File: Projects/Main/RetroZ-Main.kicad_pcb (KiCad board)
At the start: 2 copper layers, 100 x 80 mm, 22 parts, among them J1 PJ-102A, J2 Master Bus, SW1 On/Off, SW2 RESET, U1 74HCT04, U2 L7805CV-DG, U3 Z80CPU, U4 max699cpa, Y1 7.3728Mhz

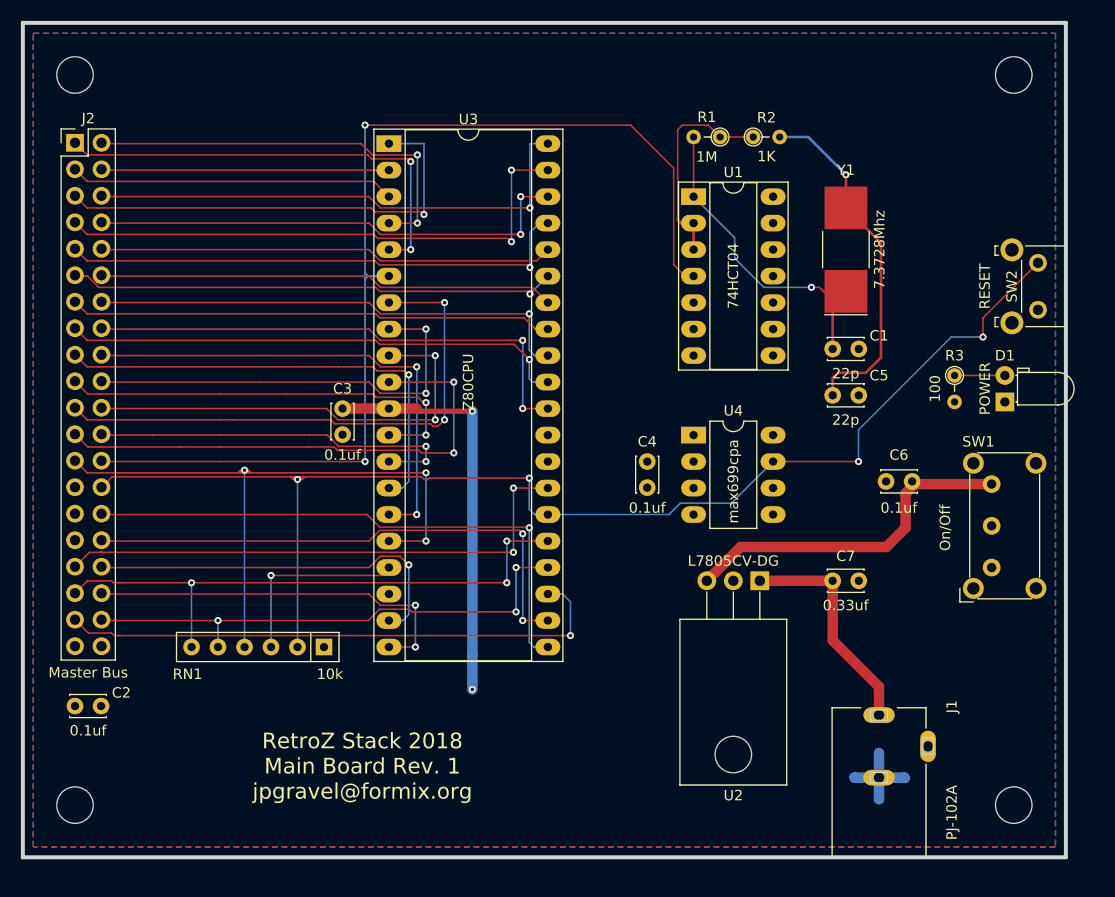
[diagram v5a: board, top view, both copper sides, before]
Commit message: fixed a bunch of issues with the main board and some on the memory board
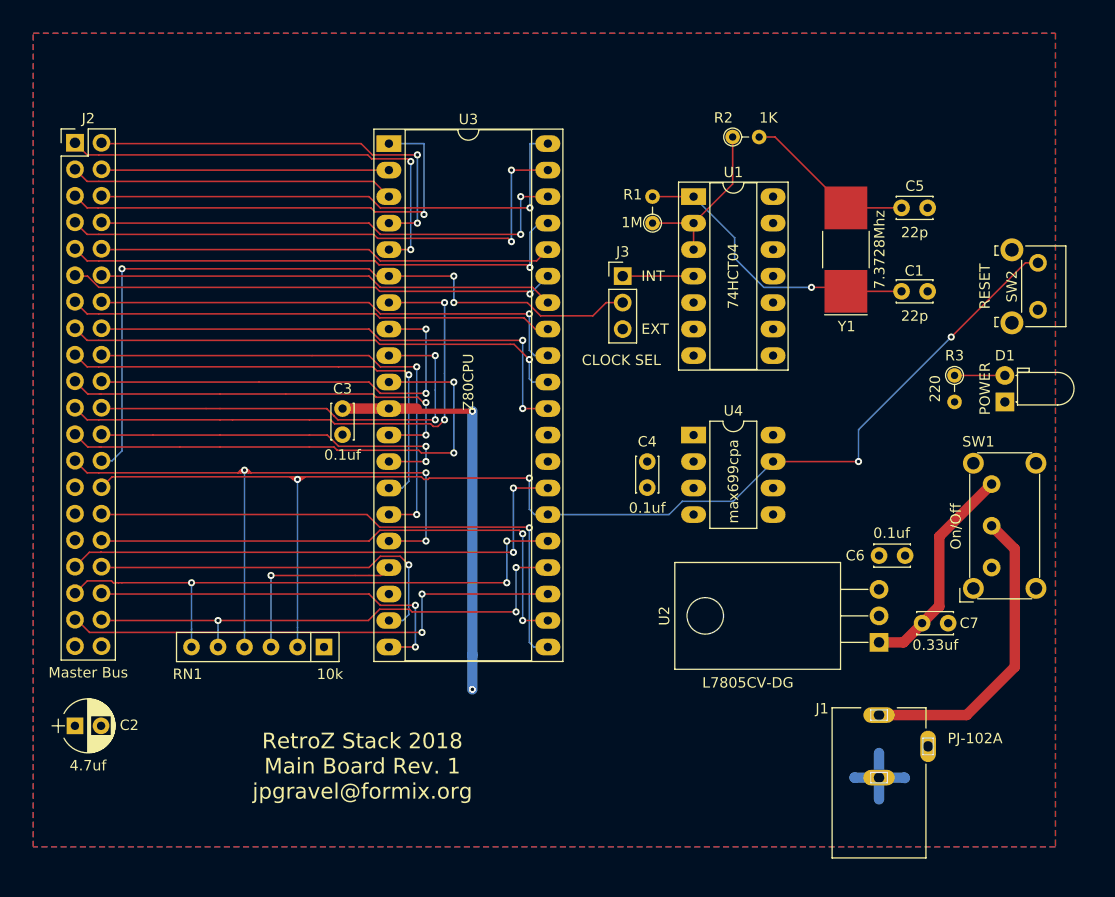
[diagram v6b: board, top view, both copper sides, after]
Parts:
- removed REF**: EuroBoard_halb_Type-I_100mmX80mm_holes, EuroBoard_Outline:EuroBoard_halb_Type-I_100mmX80mm_holes
- added J3: CLOCK SEL, Pin_Headers:Pin_Header_Straight_1x03_Pitch2.54mm, F.Cu at (147.5, 81.3)
- C2: value 0.1uf -> 4.7uf; footprint Capacitors_THT:C_Disc_D3.4mm_W2.1mm_P2.50mm -> Capacitors_THT:CP_Radial_D5.0mm_P2.50mm
- R3: value 100 -> 220
- moved C5 19.1 mm to (174.2, 74.7)
- moved U2 12.9 mm to (172.1, 116.4), turned to 90 degrees
- moved R1 10.5 mm to (150.4, 76.2), turned to 90 degrees
- moved C7 9.49 mm to (176.2, 114.6)
- moved C1 8.61 mm to (174.2, 82.7)
- moved C6 7.79 mm to (172.1, 108.1), turned to 0 degrees
- moved R2 1.97 mm to (158.1, 67.9)
- moved C2 1.90 mm to (95.0, 124.4)
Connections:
- C6 pad 1: Net-(C6-Pad1) -> VCC
- J1 pad 1: Net-(C7-Pad1) -> Net-(J1-Pad1)
- SW1 pad 2: VCC -> Net-(J1-Pad1)
- SW1 pad 3: Net-(C6-Pad1) -> Net-(C7-Pad1)
- U1 pad 4: CLK -> Net-(J3-Pad1)
- U2 pad 3: Net-(C6-Pad1) -> VCC
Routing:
- net Net-(C6-Pad1): track 33.1 -> 0.00 mm
- net CLK: track 103.8 -> 71.7 mm, vias 2 -> 3
- net Net-(J1-Pad1): track 0.00 -> 29.4 mm
- net Net-(C5-Pad1): track 34.3 -> 16.5 mm, vias 1 -> 0
- net Net-(J3-Pad1): track 0.00 -> 7.68 mm
- net ~BUSACK: track 53.9 -> 49.5 mm, vias 1 -> 2
- net Net-(R1-Pad1): track 20.7 -> 17.2 mm
- net ~RESET: track 125.5 -> 124.4 mm
- net Net-(C1-Pad1): track 31.8 -> 31.1 mm
- net Net-(C7-Pad1): track 21.7 -> 21.1 mm
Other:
- board size 100 x 80 mm -> 6 x 7 mm
- board text added: "EXT"
- board text added: "INT"

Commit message: changed power-on reser chip
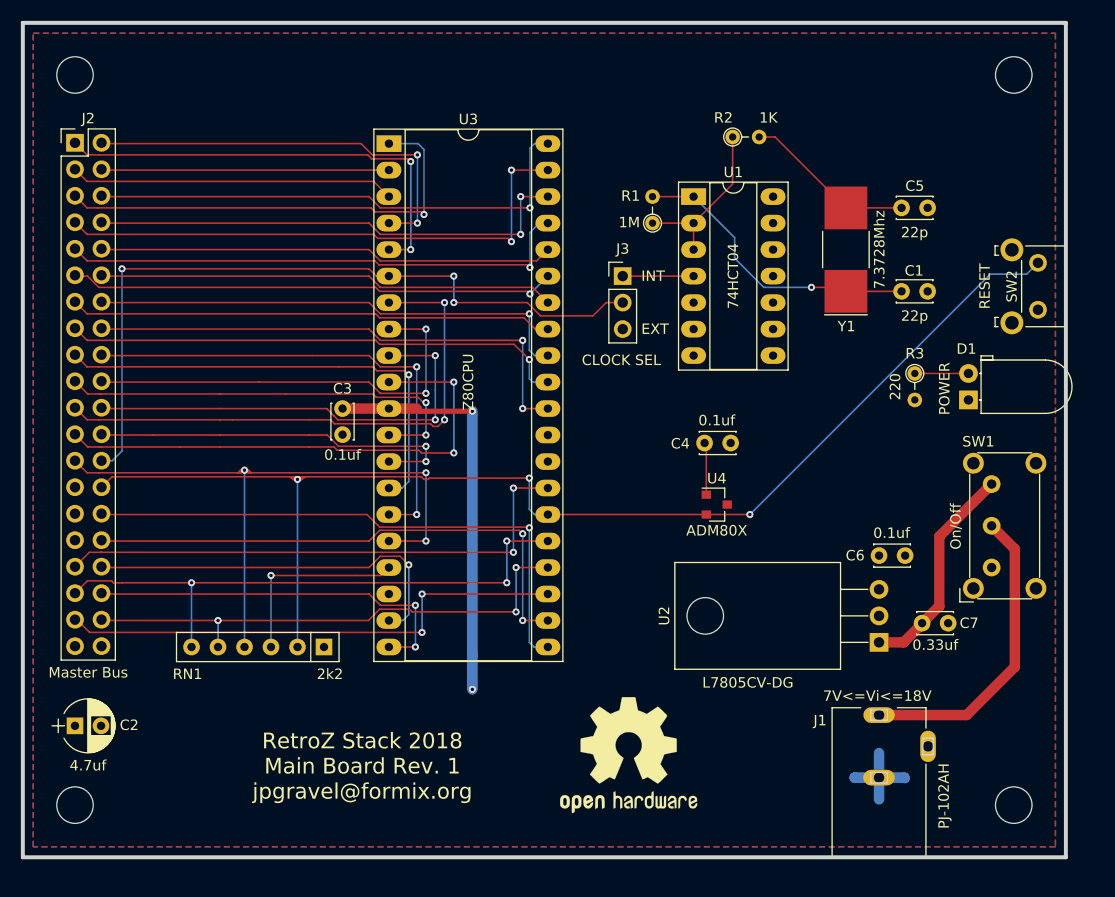
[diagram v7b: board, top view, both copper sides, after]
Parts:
- added REF**: EuroBoard_halb_Type-I_100mmX80mm_holes, EuroBoard_Outline:EuroBoard_halb_Type-I_100mmX80mm_holes, F.Cu at (90.0, 137.0)
- added REF***: OSHW-Logo2_14.6x12mm_SilkScreen, Symbols:OSHW-Logo2_14.6x12mm_SilkScreen, F.Cu at (148.1, 127.2)
- D1: footprint LEDs:LED_D3.0mm_Horizontal_O1.27mm_Z2.0mm -> LEDs:LED_D5.0mm_Horizontal_O1.27mm_Z3.0mm
- J1: value PJ-102A -> PJ-102AH
- RN1: value 10k -> 2k2
- U4: value max699cpa -> ADM80X; footprint Housings_DIP:DIP-8_W7.62mm_LongPads -> TO_SOT_Packages_SMD:SOT-23
- moved C4 8.20 mm to (157.9, 97.3), turned to 180 degrees
- moved U4 7.03 mm to (156.5, 103.2)
- moved R3 3.81 mm to (175.5, 90.6)
- moved D1 3.50 mm to (180.7, 93.2)
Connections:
- U4 pad 1: VCC -> GND
- U4 pad 2: VCC -> ~RESET
- U4 pad 3: GND -> VCC
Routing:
- net GND: track 9.30 -> 14.3 mm
- net ~RESET: track 124.4 -> 122.6 mm, vias 4 -> 3
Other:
- board size 6 x 7 mm -> 100 x 80 mm
- board text added: "7V<=Vi<=18V"

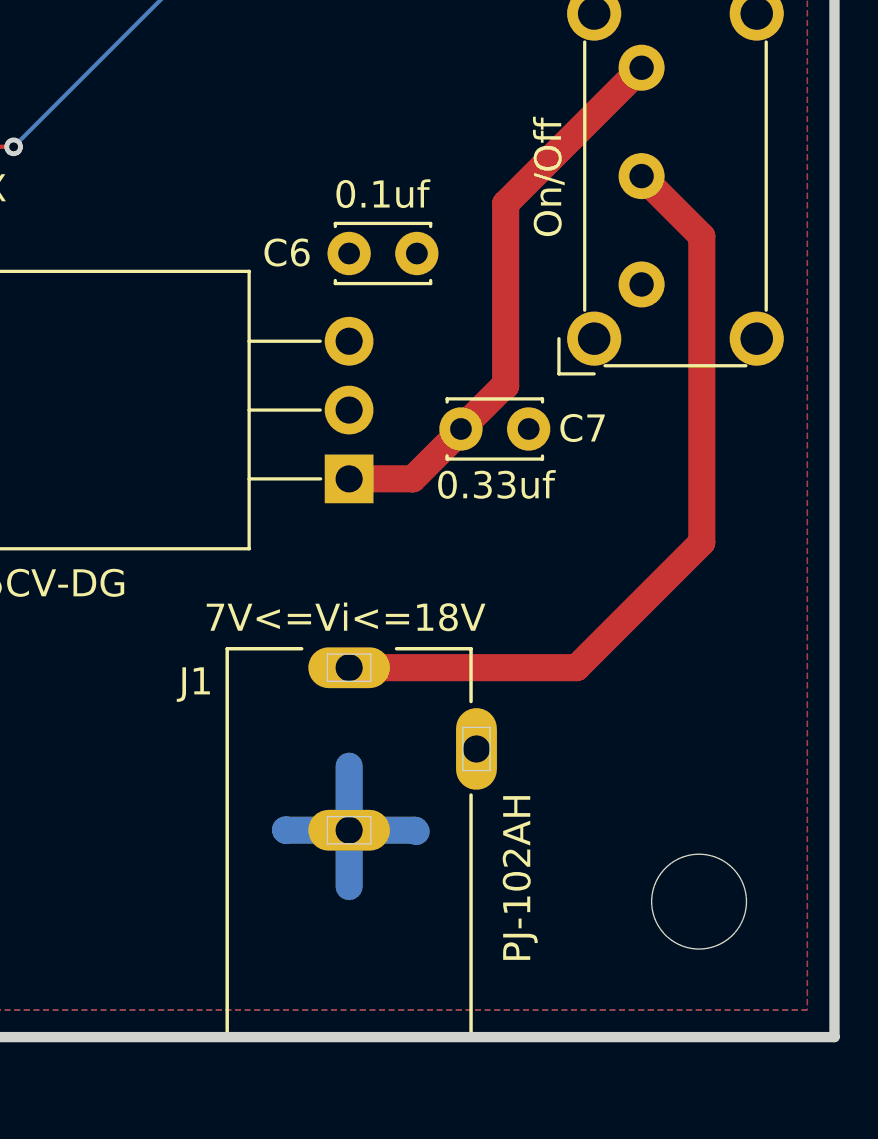
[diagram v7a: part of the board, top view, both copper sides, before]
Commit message: fixing memory access time
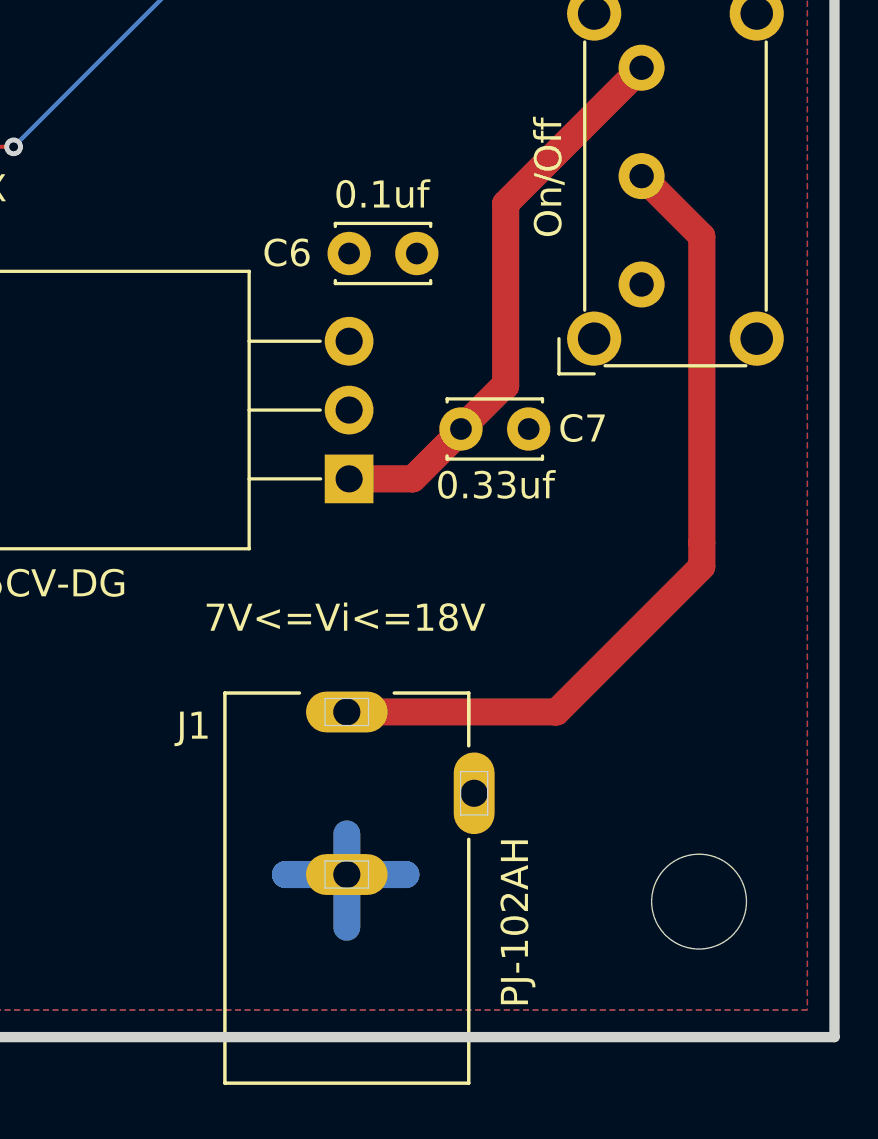
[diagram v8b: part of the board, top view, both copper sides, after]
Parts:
- moved J1 1.64 mm to (172.0, 128.0)
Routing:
- net GND: track 14.3 -> 12.9 mm
- net Net-(J1-Pad1): track 29.4 -> 30.7 mm
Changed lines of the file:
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@@
     (thickness 1.6)
     (drawings 4)
-    (tracks 432)
+    (tracks 433)
     (zones 0)
     (modules 24)
@@
   )
   (setup
-    (last_trace_width 0.1524)
+    (last_trace_width 1)
     (user_trace_width 0.254)
     (user_trace_width 0.5)
@@
       (drillshape 0)
       (scaleselection 1)
-      (outputdirectory ../plots/RetroZ-Main))
+      (outputdirectory ../../plots/RetroZ-Main/))
   )
   (net 0 "")
@@
   )
   (module PJ-102A:CUI_PJ-102A (layer Top)
-    (at 172.085 126.365 180)
+    (at 172 128 180)
     (fp_text reference J1 (at 5.6515 2.4765 360) (layer F.SilkS)
       (effects (font (size 1 1) (thickness 0.15)))
@@
   (segment (start 167.64 84.01) (end 168.91 82.74) (width 0.254) (layer Top) (net 1))
   (segment (start 168.5295 82.3595) (end 168.91 82.74) (width 0.254) (layer Top) (net 1))
+  (segment (start 172 131) (end 169.736 131) (width 1) (layer Bottom) (net 2) (status 400000))
+  (segment (start 169.736 131) (end 169.7355 131.0005) (width 1) (layer Bottom) (net 2))
+  (segment (start 172 131) (end 174.18 131) (width 1) (layer Bottom) (net 2) (status 400000))
+  (segment (start 174.18 131) (end 174.1805 131.0005) (width 1) (layer Bottom) (net 2))
+  (segment (start 172 131) (end 172 132.9475) (width 1) (layer Bottom) (net 2) (status 400000))
+  (segment (start 172 131) (end 172 129.498) (width 1) (layer Bottom) (net 2) (status 400000))
   (segment (start 155.5275 102.2375) (end 155.5275 97.4485) (width 0.1524) (layer Top) (net 2))
   (segment (start 155.5275 97.4485) (end 155.361 97.282) (width 0.1524) (layer Top) (net 2))
-  (segment (start 172.085 129.365) (end 169.751 129.365) (width 1) (layer Bottom) (net 2))
-  (segment (start 169.751 129.365) (end 169.7355 129.3495) (width 1) (layer Bottom) (net 2))
-  (segment (start 172.085 129.365) (end 174.5135 129.365) (width 1) (layer Bottom) (net 2))
-  (segment (start 174.5135 129.365) (end 174.5615 129.413) (width 1) (layer Bottom) (net 2))
-  (segment (start 172.085 129.365) (end 172.085 131.445) (width 1) (layer Bottom) (net 2))
-  (segment (start 172.085 129.365) (end 172.085 127) (width 1) (layer Bottom) (net 2))
   (segment (start 125.095 93.98) (end 127.762 93.98) (width 1) (layer Top) (net 3))
   (via (at 133.096 120.904) (size 0.6858) (drill 0.3302) (layers Top Bottom) (net 3))
@@
   (segment (start 113.792 116.84) (end 113.792 109.982) (width 0.1524) (layer Bottom) (net 50))
   (segment (start 124.333 109.982) (end 125.095 109.22) (width 0.1524) (layer Top) (net 50))
-  (segment (start 172.085 123.365) (end 180.4825 123.365) (width 1) (layer Top) (net 51))
-  (segment (start 185.1025 107.4425) (end 182.88 105.22) (width 1) (layer Top) (net 51))
+  (segment (start 185.1025 118.745) (end 185.1025 119.634) (width 1) (layer Top) (net 51))
   (segment (start 185.1025 118.745) (end 185.1025 107.4425) (width 1) (layer Top) (net 51))
-  (segment (start 180.4825 123.365) (end 185.1025 118.745) (width 1) (layer Top) (net 51))
+  (segment (start 182.88 105.22) (end 185.1025 107.4425) (width 1) (layer Top) (net 51))
+  (segment (start 179.7365 125) (end 172 125) (width 1) (layer Top) (net 51) (status 800000))
+  (segment (start 185.1025 119.634) (end 179.7365 125) (width 1) (layer Top) (net 51))
   (segment (start 147.5105 81.28) (end 154.305 81.28) (width 0.1524) (layer Top) (net 52))
   (segment (start 154.305 81.28) (end 154.305 81.3435) (width 0.1524) (layer Bottom) (net 52))
